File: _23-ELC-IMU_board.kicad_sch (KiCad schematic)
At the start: 9 parts

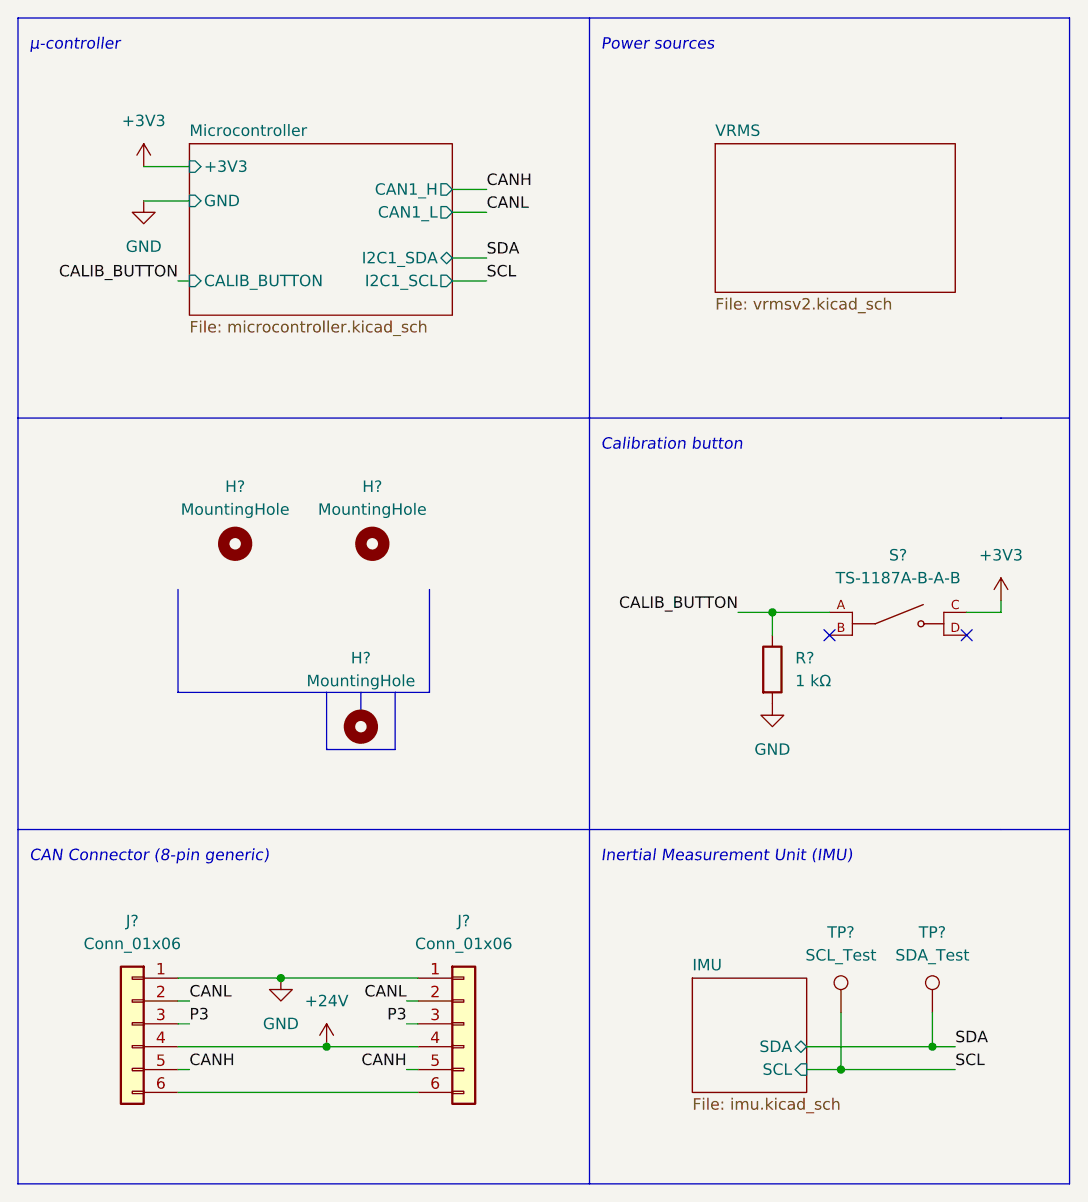
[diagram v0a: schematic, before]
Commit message: Added 3x1 connector for logical analyzer
Idk how to denote a 3-pin header
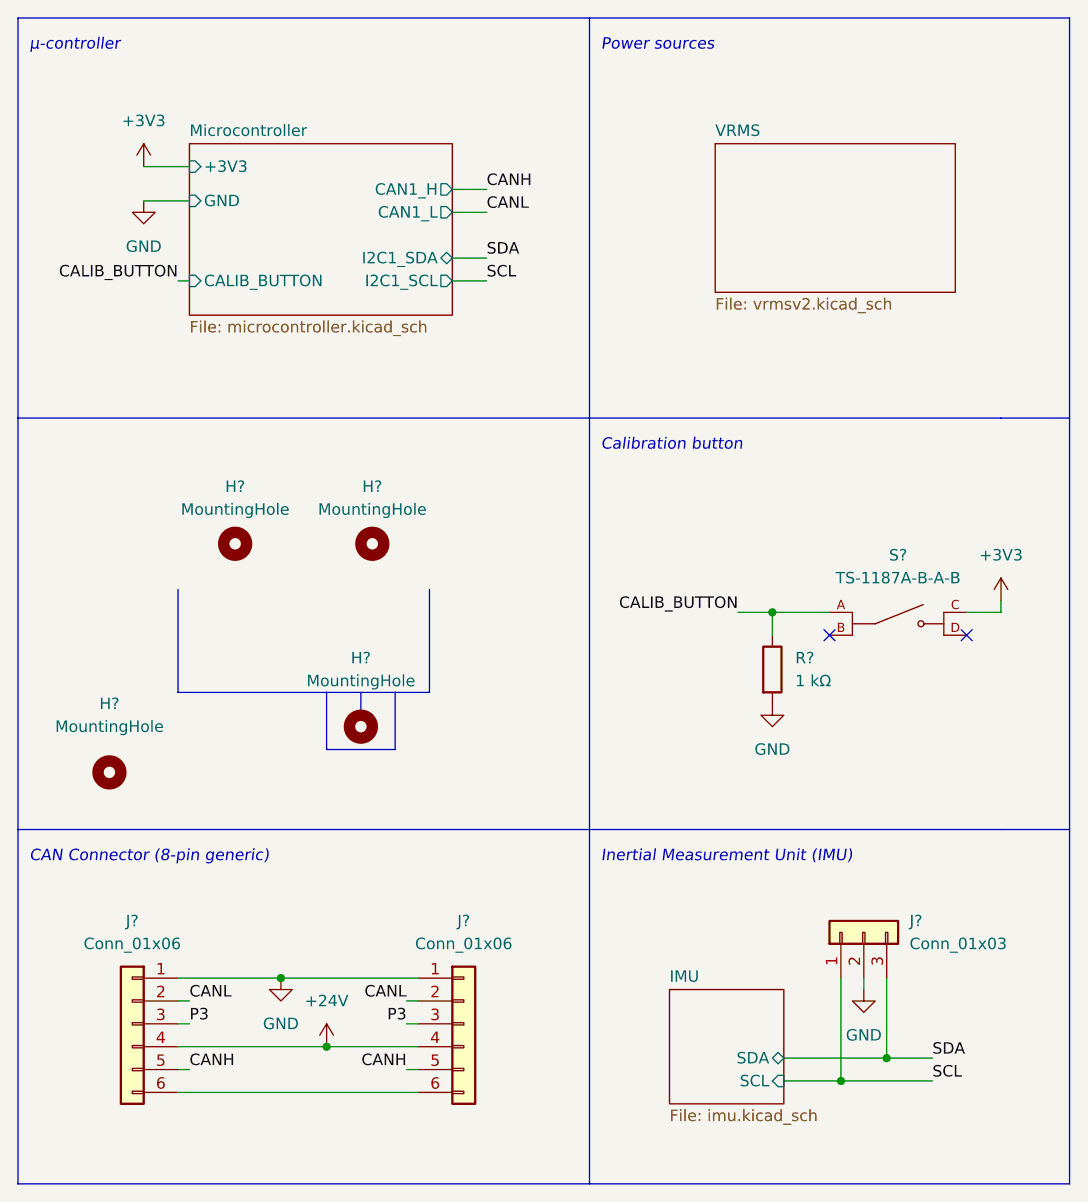
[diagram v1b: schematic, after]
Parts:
- removed TP?: SDA_Test, symbol Connector:TestPoint
- removed TP?: SCL_Test, symbol Connector:TestPoint
- added H?: MountingHole, symbol Mechanical:MountingHole
- added J?: Conn_01x03, symbol Connector_Generic:Conn_01x03
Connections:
- net GND: now also J?.2 (Pin_2)
- net SCL: now also J?.1 (Pin_1)
- net SDA: now also J?.3 (Pin_3)
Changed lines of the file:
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@@
   (junction (at 130.81 143.51) (diameter 0) (color 0 0 0 0)
   )
+  (junction (at 187.96 147.32) (diameter 0) (color 0 0 0 0)
+  )
   (junction (at 180.34 95.25) (diameter 0) (color 0 0 0 0)
   )
   (junction (at 125.73 135.89) (diameter 0) (color 0 0 0 0)
   )
-  (junction (at 187.96 146.05) (diameter 0) (color 0 0 0 0)
-  )
-  (junction (at 198.12 143.51) (diameter 0) (color 0 0 0 0)
+  (junction (at 193.04 144.78) (diameter 0) (color 0 0 0 0)
   )
   (no_connect (at 201.93 97.79))
@@
     (stroke (width 0) (type default) (color 0 0 0 0))
   )
-  (wire (pts (xy 198.12 139.7) (xy 198.12 143.51))
-    (stroke (width 0) (type default) (color 0 0 0 0))
-  )
   (wire (pts (xy 114.3 146.05) (xy 115.57 146.05))
     (stroke (width 0) (type default) (color 0 0 0 0))
@@
     (stroke (width 0) (type default) (color 0 0 0 0))
   )
+  (wire (pts (xy 193.04 144.78) (xy 198.12 144.78))
+    (stroke (width 0) (type default) (color 0 0 0 0))
+  )
   (polyline (pts (xy 134.62 104.14) (xy 134.62 106.68))
     (stroke (width 0) (type default) (color 0 0 0 0))
@@
     (stroke (width 0) (type default) (color 0 0 0 0))
   )
+  (wire (pts (xy 193.04 135.89) (xy 193.04 144.78))
+    (stroke (width 0) (type default) (color 0 0 0 0))
+  )
   (wire (pts (xy 110.49 49.53) (xy 115.57 49.53))
     (stroke (width 0) (type default) (color 0 0 0 0))
@@
     (stroke (width 0) (type default) (color 0 0 0 0))
   )
+  (wire (pts (xy 190.5 137.16) (xy 190.5 135.89))
+    (stroke (width 0) (type default) (color 0 0 0 0))
+  )
   (polyline (pts (xy 114.3 92.71) (xy 114.3 104.14))
     (stroke (width 0) (type default) (color 0 0 0 0))
   )
+  (wire (pts (xy 187.96 135.89) (xy 187.96 147.32))
+    (stroke (width 0) (type default) (color 0 0 0 0))
+  )
   (wire (pts (xy 114.3 148.59) (xy 140.97 148.59))
     (stroke (width 0) (type default) (color 0 0 0 0))
@@
     (stroke (width 0) (type default) (color 0 0 0 0))
   )
-  (wire (pts (xy 187.96 146.05) (xy 200.66 146.05))
-    (stroke (width 0) (type default) (color 0 0 0 0))
-  )
   (polyline (pts (xy 96.52 73.66) (xy 160.02 73.66))
     (stroke (width 0) (type default) (color 0 0 0 0))
@@
     (stroke (width 0) (type default) (color 0 0 0 0))
   )
-  (wire (pts (xy 184.15 143.51) (xy 198.12 143.51))
-    (stroke (width 0) (type default) (color 0 0 0 0))
-  )
   (polyline (pts (xy 96.52 119.38) (xy 160.02 119.38))
     (stroke (width 0) (type default) (color 0 0 0 0))
@@
     (stroke (width 0) (type default) (color 0 0 0 0))
   )
-  (wire (pts (xy 187.96 139.7) (xy 187.96 146.05))
-    (stroke (width 0) (type default) (color 0 0 0 0))
-  )
   (polyline (pts (xy 96.52 29.21) (xy 213.36 29.21))
     (stroke (width 0) (type default) (color 0 0 0 0))
@@
     (stroke (width 0) (type default) (color 0 0 0 0))
   )
+  (wire (pts (xy 187.96 147.32) (xy 198.12 147.32))
+    (stroke (width 0) (type default) (color 0 0 0 0))
+  )
   (polyline (pts (xy 138.43 110.49) (xy 138.43 104.14))
     (stroke (width 0) (type default) (color 0 0 0 0))
@@
     (stroke (width 0) (type default) (color 0 0 0 0))
   )
-  (wire (pts (xy 184.15 146.05) (xy 187.96 146.05))
+  (wire (pts (xy 181.61 147.32) (xy 187.96 147.32))
     (stroke (width 0) (type default) (color 0 0 0 0))
   )
@@
     (stroke (width 0) (type default) (color 0 0 0 0))
   )
-  (wire (pts (xy 198.12 143.51) (xy 200.66 143.51))
+  (wire (pts (xy 181.61 144.78) (xy 193.04 144.78))
     (stroke (width 0) (type default) (color 0 0 0 0))
   )
@@
     (effects (font (size 1.27 1.27) italic) (justify left bottom))
   )
-  (label "SDA" (at 200.66 143.51 0)
+  (label "SDA" (at 198.12 144.78 0)
     (effects (font (size 1.27 1.27)) (justify left bottom))
   )
@@
     (effects (font (size 1.27 1.27)) (justify left bottom))
   )
-  (label "SCL" (at 200.66 146.05 0)
+  (label "SCL" (at 198.12 147.32 0)
     (effects (font (size 1.27 1.27)) (justify left bottom))
   )
@@
     (pin "1")
   )
-  (symbol (lib_id "Connector:TestPoint") (at 198.12 139.7 0) (unit 1)
-    (in_bom yes) (on_board yes)
-    (property "Reference" "TP?" (id 0) (at 198.12 130.81 0))
-    (property "Value" "SDA_Test" (id 1) (at 198.12 133.35 0))
-    (property "Footprint" "" (id 2) (at 203.2 139.7 0)
-      (effects (font (size 1.27 1.27)) hide)
-    )
-    (property "Datasheet" "~" (id 3) (at 203.2 139.7 0)
-      (effects (font (size 1.27 1.27)) hide)
-    )
-    (pin "1")
-  )
   (symbol (lib_id "Mechanical:MountingHole") (at 120.65 87.63 0) (unit 1)
     (in_bom yes) (on_board yes)
@@
     (pin "1")
   )
+  (symbol (lib_id "Connector_Generic:Conn_01x03") (at 190.5 130.81 90) (unit 1)
+    (in_bom yes) (on_board yes) (fields_autoplaced)
+    (property "Reference" "J?" (id 0) (at 195.58 129.5399 90)
+      (effects (font (size 1.27 1.27)) (justify right))
+    )
+    (property "Value" "Conn_01x03" (id 1) (at 195.58 132.0799 90)
+      (effects (font (size 1.27 1.27)) (justify right))
+    )
+    (property "Footprint" "" (id 2) (at 190.5 130.81 0)
+      (effects (font (size 1.27 1.27)) hide)
+    )
+    (property "Datasheet" "~" (id 3) (at 190.5 130.81 0)
+      (effects (font (size 1.27 1.27)) hide)
+    )
+    (pin "1")
+    (pin "2")
+    (pin "3")
+  )
   (symbol (lib_id "Mechanical:MountingHole") (at 134.62 107.95 0) (unit 1)
     (in_bom yes) (on_board yes)
@@
     (pin "1")
   )
-  (symbol (lib_id "Connector:TestPoint") (at 187.96 139.7 0) (unit 1)
+  (symbol (lib_id "power:GND") (at 190.5 137.16 0) (unit 1)
+    (in_bom yes) (on_board yes) (fields_autoplaced)
+    (property "Reference" "#PWR?" (id 0) (at 190.5 143.51 0)
+      (effects (font (size 1.27 1.27)) hide)
+    )
+    (property "Value" "GND" (id 1) (at 190.5 142.24 0))
+    (property "Footprint" "" (id 2) (at 190.5 137.16 0)
+      (effects (font (size 1.27 1.27)) hide)
+    )
+    (property "Datasheet" "" (id 3) (at 190.5 137.16 0)
+      (effects (font (size 1.27 1.27)) hide)
+    )
+    (pin "1")
+  )
+  (symbol (lib_id "Mechanical:MountingHole") (at 106.68 113.03 0) (unit 1)
     (in_bom yes) (on_board yes)
-    (property "Reference" "TP?" (id 0) (at 187.96 130.81 0))
-    (property "Value" "SCL_Test" (id 1) (at 187.96 133.35 0))
-    (property "Footprint" "" (id 2) (at 193.04 139.7 0)
-      (effects (font (size 1.27 1.27)) hide)
-    )
-    (property "Datasheet" "~" (id 3) (at 193.04 139.7 0)
-      (effects (font (size 1.27 1.27)) hide)
-    )
-    (pin "1")
+    (property "Reference" "H?" (id 0) (at 106.68 105.41 0))
+    (property "Value" "MountingHole" (id 1) (at 106.68 107.95 0))
+    (property "Footprint" "" (id 2) (at 106.68 113.03 0)
+      (effects (font (size 1.27 1.27)) hide)
+    )
+    (property "Datasheet" "~" (id 3) (at 106.68 113.03 0)
+      (effects (font (size 1.27 1.27)) hide)
+    )
   )
   (symbol (lib_id "power:GND") (at 110.49 49.53 0) (unit 1)
@@
     )
   )
-  (sheet (at 171.45 135.89) (size 12.7 12.7) (fields_autoplaced)
+  (sheet (at 168.91 137.16) (size 12.7 12.7) (fields_autoplaced)
     (stroke (width 0.1524) (type solid) (color 0 0 0 0))
     (fill (color 0 0 0 0.0000))
-    (property "Sheet name" "IMU" (id 0) (at 171.45 135.1784 0)
+    (property "Sheet name" "IMU" (id 0) (at 168.91 136.4484 0)
       (effects (font (size 1.27 1.27)) (justify left bottom))
     )
-    (property "Sheet file" "imu.kicad_sch" (id 1) (at 171.45 149.1746 0)
+    (property "Sheet file" "imu.kicad_sch" (id 1) (at 168.91 150.4446 0)
       (effects (font (size 1.27 1.27)) (justify left top))
     )
-    (pin "SDA" bidirectional (at 184.15 143.51 0)
+    (pin "SDA" bidirectional (at 181.61 144.78 0)
       (effects (font (size 1.27 1.27)) (justify right))
     )
-    (pin "SCL" input (at 184.15 146.05 0)
+    (pin "SCL" input (at 181.61 147.32 0)
       (effects (font (size 1.27 1.27)) (justify right))
     )
@@
       (reference "#PWR?") (unit 1) (value "+3V3") (footprint "")
     )
+    (path "/ced56753-f485-4bd5-be89-d8aff523a75f"
+      (reference "#PWR?") (unit 1) (value "GND") (footprint "")
+    )
     (path "/fc2246ca-4cc5-401c-a2d9-9f0b303097a4"
       (reference "#PWR?") (unit 1) (value "GND") (footprint "")
@@
       (reference "H?") (unit 1) (value "MountingHole") (footprint "")
     )
+    (path "/ddcbeaef-7344-4f34-8775-b1d1f0415ae7"
+      (reference "H?") (unit 1) (value "MountingHole") (footprint "")
+    )
     (path "/54e69940-e60b-406d-b33c-8246d242800f/27fec5df-f50a-420e-8f18-082a387b0bca"
       (reference "J1") (unit 1) (value "Conn_01x02") (footprint "Connector_PinHeader_2.54mm:PinHeader_1x02_P2.54mm_Vertical")
@@
       (reference "J?") (unit 1) (value "Conn_01x06") (footprint "")
     )
+    (path "/5fe97024-2e49-4443-bc0c-2f1272ffe457"
+      (reference "J?") (unit 1) (value "Conn_01x03") (footprint "")
+    )
     (path "/98f8d048-5fd0-450e-921f-559b233f72a7"
       (reference "J?") (unit 1) (value "Conn_01x06") (footprint "")
@@
       (reference "TP7") (unit 1) (value " ") (footprint "TestPoint:TestPoint_THTPad_1.0x1.0mm_Drill0.5mm")
     )
-    (path "/2e20534c-db23-4779-b935-bdcdad748d27"
-      (reference "TP?") (unit 1) (value "SDA_Test") (footprint "")
-    )
-    (path "/f5a8a556-7cb0-4bdc-b114-48db54953dd2"
-      (reference "TP?") (unit 1) (value "SCL_Test") (footprint "")
-    )
     (path "/54e69940-e60b-406d-b33c-8246d242800f/00000000-0000-0000-0000-0000634311a7"

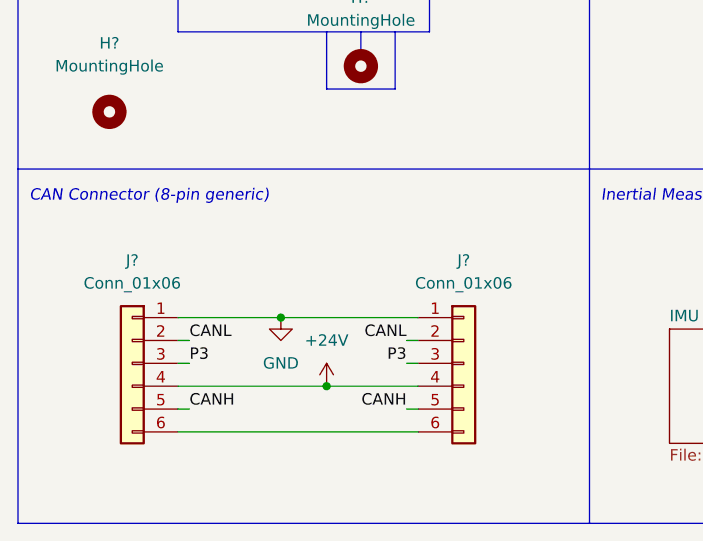
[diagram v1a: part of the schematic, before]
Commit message: Removed analog filtering
There are no analog parts in this PCB
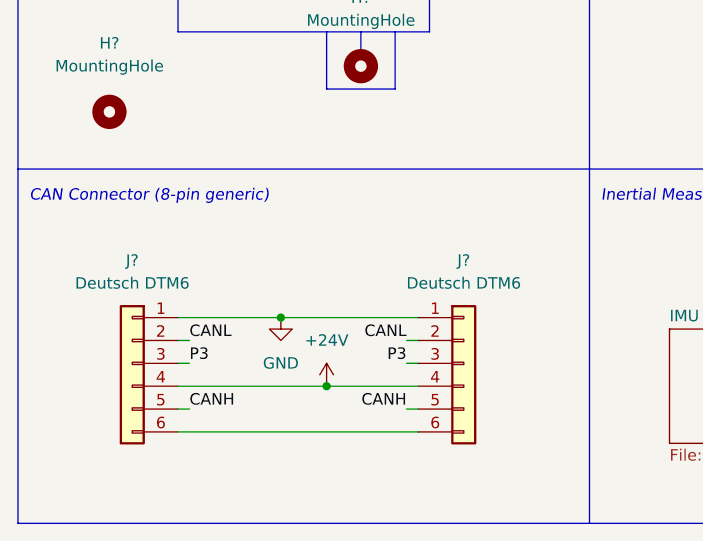
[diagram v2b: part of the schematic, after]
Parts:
- J? (x2): value Conn_01x06 -> Deutsch DTM6
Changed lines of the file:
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@@
     (in_bom yes) (on_board yes)
     (property "Reference" "J?" (id 0) (at 146.05 129.54 0))
-    (property "Value" "Conn_01x06" (id 1) (at 146.05 132.08 0))
+    (property "Value" "Deutsch DTM6" (id 1) (at 146.05 132.08 0))
     (property "Footprint" "" (id 2) (at 146.05 140.97 0)
       (effects (font (size 1.27 1.27)) hide)
@@
     (in_bom yes) (on_board yes) (fields_autoplaced)
     (property "Reference" "J?" (id 0) (at 109.22 129.54 0))
-    (property "Value" "Conn_01x06" (id 1) (at 109.22 132.08 0))
+    (property "Value" "Deutsch DTM6" (id 1) (at 109.22 132.08 0))
     (property "Footprint" "" (id 2) (at 109.22 140.97 0)
       (effects (font (size 1.27 1.27)) hide)
@@
       (reference "#PWR010") (unit 1) (value "+3V3") (footprint "")
     )
-    (path "/54e69940-e60b-406d-b33c-8246d242800f/20ea3bd5-4e5a-42ee-badd-a960f97ca70d"
-      (reference "#PWR011") (unit 1) (value "+3V3") (footprint "")
-    )
     (path "/54e69940-e60b-406d-b33c-8246d242800f/d193e015-664a-4a56-b639-1ea10c5180a7"
       (reference "#PWR012") (unit 1) (value "GND") (footprint "")
@@
       (reference "#PWR014") (unit 1) (value "GND") (footprint "")
     )
-    (path "/54e69940-e60b-406d-b33c-8246d242800f/00000000-0000-0000-0000-00006345342b"
-      (reference "#PWR015") (unit 1) (value "GND") (footprint "")
-    )
     (path "/54e69940-e60b-406d-b33c-8246d242800f/d6f96a49-6f78-47db-8cff-86585c8d7dc4"
       (reference "#PWR016") (unit 1) (value "+3V3") (footprint "")
@@
       (reference "#PWR017") (unit 1) (value "GND") (footprint "")
     )
-    (path "/54e69940-e60b-406d-b33c-8246d242800f/00000000-0000-0000-0000-00006344e612"
-      (reference "#PWR020") (unit 1) (value "+3.3VA") (footprint "")
-    )
     (path "/54e69940-e60b-406d-b33c-8246d242800f/6dc19955-c028-4686-acb6-6e23df83336f"
       (reference "#PWR021") (unit 1) (value "GND") (footprint "")
@@
       (reference "C6") (unit 1) (value "100nF") (footprint "Capacitor_SMD:C_0603_1608Metric_Pad1.08x0.95mm_HandSolder")
     )
-    (path "/54e69940-e60b-406d-b33c-8246d242800f/00000000-0000-0000-0000-00006344ff92"
-      (reference "C7") (unit 1) (value "1u") (footprint "Capacitor_SMD:C_0603_1608Metric")
-    )
     (path "/ff63b25e-ed05-40c6-94ec-12da2c4435e9/5eef7685-46e3-4490-b1c3-d367d5bf00e5/2f4ed9e2-3b6e-47a8-9b3c-3d67ddce4f56"
       (reference "C7") (unit 1) (value "22uF") (footprint "Capacitor_SMD:C_0603_1608Metric_Pad1.08x0.95mm_HandSolder")
     )
-    (path "/54e69940-e60b-406d-b33c-8246d242800f/00000000-0000-0000-0000-000063450ccd"
-      (reference "C8") (unit 1) (value "10n") (footprint "Capacitor_SMD:C_0603_1608Metric")
-    )
     (path "/ff63b25e-ed05-40c6-94ec-12da2c4435e9/5eef7685-46e3-4490-b1c3-d367d5bf00e5/0db66213-c7b5-4743-9486-49b38676a3e3"
       (reference "C8") (unit 1) (value "22uF") (footprint "Capacitor_SMD:C_0603_1608Metric_Pad1.08x0.95mm_HandSolder")
@@
     )
     (path "/09bd8a18-fa7b-4015-8547-230d491cb9a1"
-      (reference "J?") (unit 1) (value "Conn_01x06") (footprint "")
+      (reference "J?") (unit 1) (value "Deutsch DTM6") (footprint "")
     )
     (path "/5fe97024-2e49-4443-bc0c-2f1272ffe457"
@@
     )
     (path "/98f8d048-5fd0-450e-921f-559b233f72a7"
-      (reference "J?") (unit 1) (value "Conn_01x06") (footprint "")
+      (reference "J?") (unit 1) (value "Deutsch DTM6") (footprint "")
     )
     (path "/54e69940-e60b-406d-b33c-8246d242800f/af358307-4e47-4011-a445-f75ae1a48b0c"
@@
       (reference "JP2") (unit 1) (value " ") (footprint "Jumper:SolderJumper-2_P1.3mm_Bridged2Bar_Pad1.0x1.5mm")
     )
-    (path "/54e69940-e60b-406d-b33c-8246d242800f/00000000-0000-0000-0000-00006344dc34"
-      (reference "L1") (unit 1) (value "68n") (footprint "Inductor_SMD:L_0603_1608Metric")
-    )
     (path "/ff63b25e-ed05-40c6-94ec-12da2c4435e9/5eef7685-46e3-4490-b1c3-d367d5bf00e5/f2331792-5756-4679-aed2-ee592914aae4"

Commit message: Annotated schematic
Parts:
- gave numbers to parts that had none: 9
